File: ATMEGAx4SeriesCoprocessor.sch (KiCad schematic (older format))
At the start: 8 parts, among them J2 AVR-ISP-6, J3 Conn_01x06 (Serial Connector)

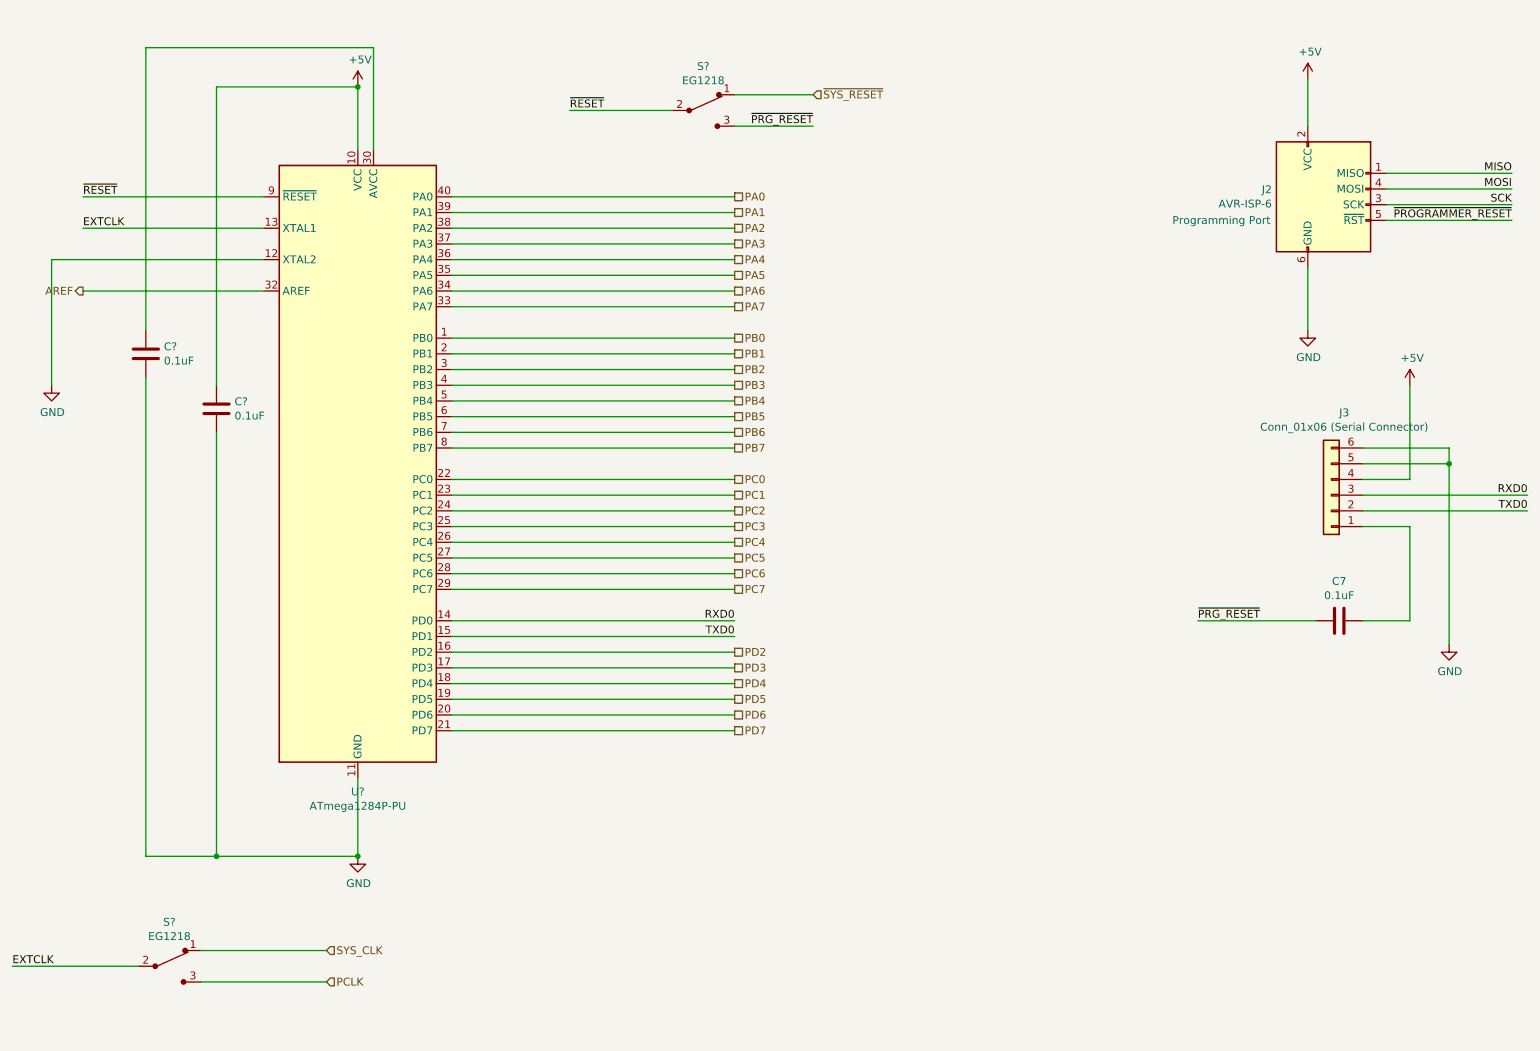
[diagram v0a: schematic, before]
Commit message: ATMEGAx4 coprocessor is basically setup
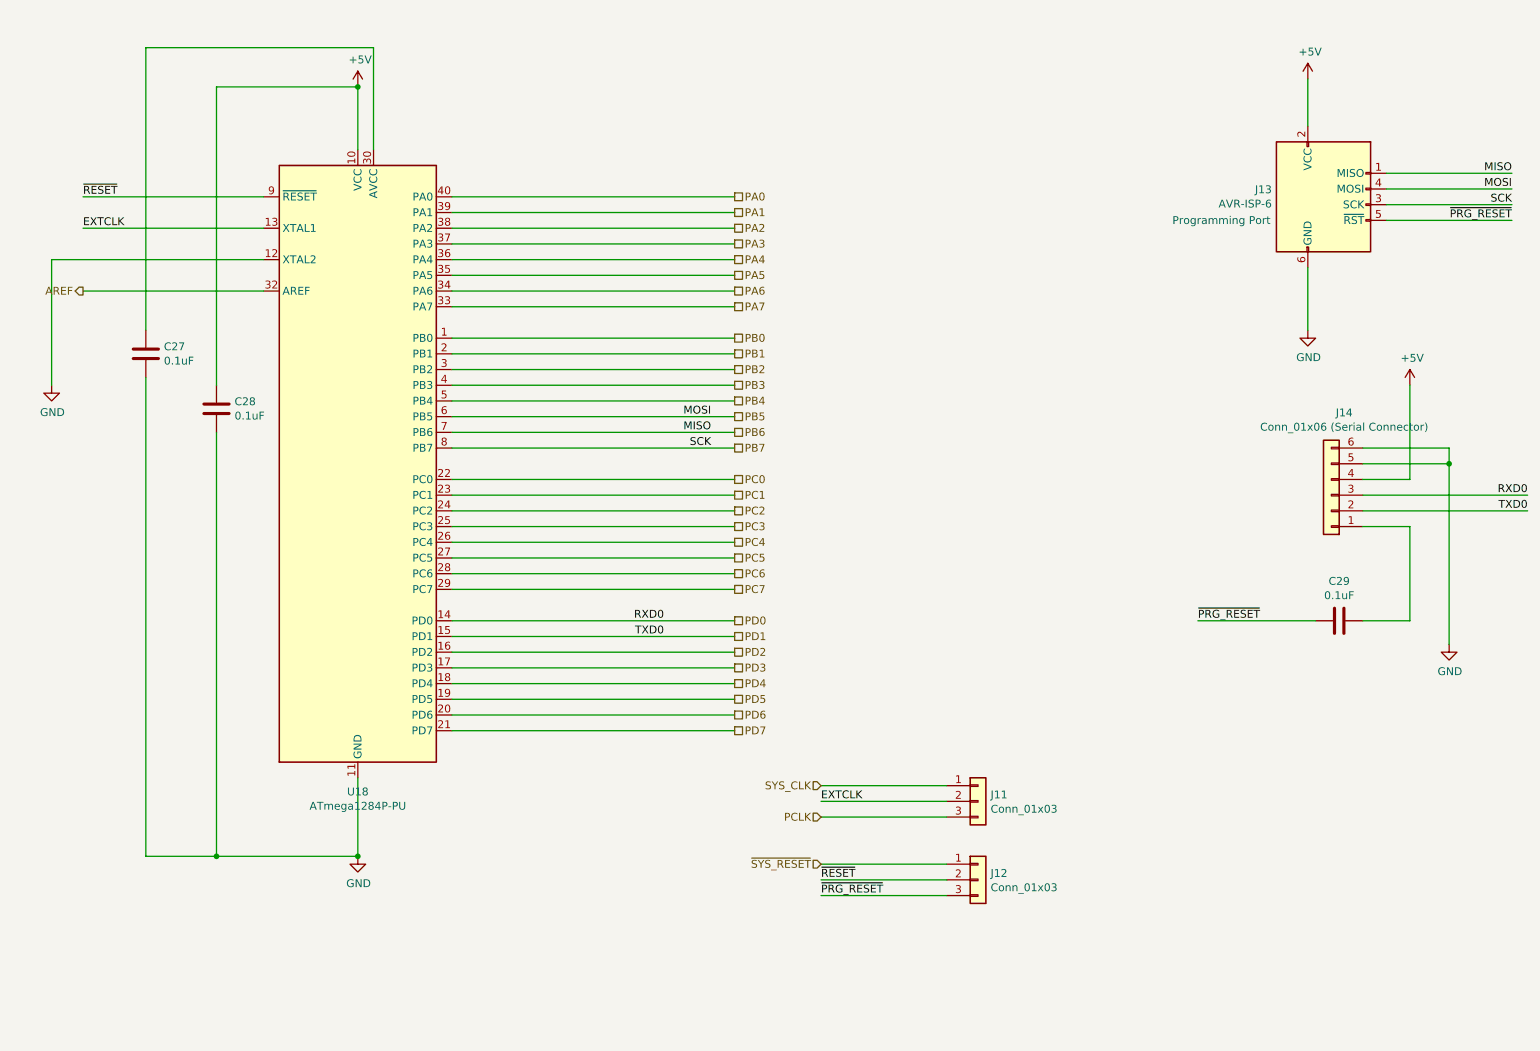
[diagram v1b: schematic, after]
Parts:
- removed S? (x2): EG1218, digikey-footprints:Switch_Slide_11.6x4mm_EG1218, symbol dk_Slide-Switches:EG1218
- added J11, J12: Conn_01x03, Connector_PinHeader_2.54mm:PinHeader_1x03_P2.54mm_Vertical, symbol Connector_Generic:Conn_01x03
- gave numbers to parts that had none: 3
- renumbered C7 to C29, J2 to J13, J3 to J14
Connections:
- net MISO is gone; now on net PB6: J13.1 (MISO)
- net MOSI is gone; now on net PB5: J13.4 (MOSI)
- net SCK is gone; now on net PB7: J13.3 (SCK)
- net ~PROGRAMMER_RESET is gone; now on net ~PRG_RESET: J13.5 (~RST)
- net EXTCLK: now also J11.2 (Pin_2)
- net PCLK: now also J11.3 (Pin_3)
- net SYS_CLK: now also J11.1 (Pin_1)
- net ~PRG_RESET: now also J12.3 (Pin_3)
- net ~RESET: now also J12.2 (Pin_2)
- net ~SYS_RESET: now also J12.1 (Pin_1)
- net RXD0 renamed PD0
- net TXD0 renamed PD1
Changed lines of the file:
@@
 $Descr A4 11693 8268
 encoding utf-8
-Sheet 4 2
+Sheet 2 2
 Title ""
 Date ""
@@
 $EndDescr
 $Comp
-L MCU_Microchip_ATmega:ATmega1284P-PU U?
+L MCU_Microchip_ATmega:ATmega1284P-PU U18
 U 1 1 7D8FC773
 P 3400 3250
-F 0 "U?" H 3400 1161 50  0000 C CNN
+F 0 "U18" H 3400 1161 50  0000 C CNN
 F 1 "ATmega1284P-PU" H 3400 1070 50  0000 C CNN
 F 2 "Package_DIP:DIP-40_W15.24mm_Socket" H 3400 3250 50  0001 C CIN
@@
 Connection ~ 3400 850
 $Comp
-L power:+5V #PWR?
+L power:+5V #PWR066
 U 1 1 7D8FC77F
 P 3400 850
-F 0 "#PWR?" H 3400 700 50  0001 C CNN
+F 0 "#PWR066" H 3400 700 50  0001 C CNN
 F 1 "+5V" H 3415 1023 50  0000 C CNN
 F 2 "" H 3400 850 50  0001 C CNN
@@
 $EndComp
 $Comp
-L power:GND #PWR?
+L power:GND #PWR067
 U 1 1 7D8FC785
 P 3400 5750
-F 0 "#PWR?" H 3400 5500 50  0001 C CNN
+F 0 "#PWR067" H 3400 5500 50  0001 C CNN
 F 1 "GND" H 3405 5577 50  0000 C CNN
 F 2 "" H 3400 5750 50  0001 C CNN
@@
 Connection ~ 3400 5750
 $Comp
-L Device:C C?
+L Device:C C27
 U 1 1 7D8FC78C
 P 2050 2550
-F 0 "C?" H 2165 2596 50  0000 L CNN
+F 0 "C27" H 2165 2596 50  0000 L CNN
 F 1 "0.1uF" H 2165 2505 50  0000 L CNN
 F 2 "" H 2088 2400 50  0001 C CNN
@@
 Connection ~ 2500 5750
 $Comp
-L Device:C C?
+L Device:C C28
 U 1 1 7D8FC798
 P 2500 2900
-F 0 "C?" H 2615 2946 50  0000 L CNN
+F 0 "C28" H 2615 2946 50  0000 L CNN
 F 1 "0.1uF" H 2615 2855 50  0000 L CNN
 F 2 "" H 2538 2750 50  0001 C CNN
@@
 	2500 3050 2500 5750
 $Comp
-L power:GND #PWR?
+L power:GND #PWR065
 U 1 1 7D8FC79F
 P 1450 2750
-F 0 "#PWR?" H 1450 2500 50  0001 C CNN
+F 0 "#PWR065" H 1450 2500 50  0001 C CNN
 F 1 "GND" H 1455 2577 50  0000 C CNN
 F 2 "" H 1450 2750 50  0001 C CNN
@@
 Wire Wire Line
 	2800 1750 1650 1750
-Text HLabel 3200 6350 2    50   Input ~ 0
+Text HLabel 6350 5300 0    50   Input ~ 0
 SYS_CLK
 Wire Wire Line
@@
 Text HLabel 5800 2850 2    50   UnSpc ~ 0
 PB4
-Text HLabel 5800 2950 2    50   UnSpc ~ 0
-PB5
-Text HLabel 5800 3050 2    50   UnSpc ~ 0
-PB6
-Text HLabel 5800 3150 2    50   UnSpc ~ 0
-PB7
 Text HLabel 5800 3350 2    50   UnSpc ~ 0
 PC0
@@
 PD7
 $Comp
-L Connector:AVR-ISP-6 J2
+L Connector:AVR-ISP-6 J13
 U 1 1 65D0C082
 P 9550 1600
-F 0 "J2" H 9221 1696 50  0000 R CNN
+F 0 "J13" H 9221 1696 50  0000 R CNN
 F 1 "AVR-ISP-6" H 9221 1605 50  0000 R CNN
 F 2 "Connector_PinHeader_2.54mm:PinHeader_2x03_P2.54mm_Vertical" V 9300 1650 50  0001 C CNN
@@
 	1    0    0    -1
 $EndComp
-Text Label 10750 1400 2    50   ~ 0
-MISO
 Text Label 10750 1500 2    50   ~ 0
 MOSI
@@
 	9450 1100 9450 800
 $Comp
-L power:+5V #PWR022
+L power:+5V #PWR068
 U 1 1 65D67928
 P 9450 800
-F 0 "#PWR022" H 9450 650 50  0001 C CNN
+F 0 "#PWR068" H 9450 650 50  0001 C CNN
 F 1 "+5V" H 9465 973 50  0000 C CNN
 F 2 "" H 9450 800 50  0001 C CNN
@@
 	9450 2000 9450 2400
 $Comp
-L power:GND #PWR023
+L power:GND #PWR069
 U 1 1 65D7AB96
 P 9450 2400
-F 0 "#PWR023" H 9450 2150 50  0001 C CNN
+F 0 "#PWR069" H 9450 2150 50  0001 C CNN
 F 1 "GND" H 9455 2227 50  0000 C CNN
 F 2 "" H 9450 2400 50  0001 C CNN
@@
 $EndComp
 $Comp
-L Connector_Generic:Conn_01x06 J3
+L Connector_Generic:Conn_01x06 J14
 U 1 1 623C8548
 P 9600 3450
-F 0 "J3" H 9518 2925 50  0000 C CNN
+F 0 "J14" H 9518 2925 50  0000 C CNN
 F 1 "Conn_01x06 (Serial Connector)" H 9518 3016 50  0000 C CNN
 F 2 "Connector_PinHeader_2.54mm:PinHeader_1x06_P2.54mm_Vertical" H 9600 3450 50  0001 C CNN
@@
 	9800 3550 10850 3550
 $Comp
-L power:+5V #PWR026
+L power:+5V #PWR070
 U 1 1 65E08A07
 P 10100 2750
-F 0 "#PWR026" H 10100 2600 50  0001 C CNN
+F 0 "#PWR070" H 10100 2600 50  0001 C CNN
 F 1 "+5V" H 10115 2923 50  0000 C CNN
 F 2 "" H 10100 2750 50  0001 C CNN
@@
 	9800 3350 10100 3350
 $Comp
-L power:GND #PWR027
+L power:GND #PWR071
 U 1 1 65DF3F8A
 P 10350 4400
-F 0 "#PWR027" H 10350 4150 50  0001 C CNN
+F 0 "#PWR071" H 10350 4150 50  0001 C CNN
 F 1 "GND" H 10355 4227 50  0000 C CNN
 F 2 "" H 10350 4400 50  0001 C CNN
@@
 	8750 4250 9500 4250
 $Comp
-L Device:C C7
+L Device:C C29
 U 1 1 65D916C2
 P 9650 4250
-F 0 "C7" V 9398 4250 50  0000 C CNN
+F 0 "C29" V 9398 4250 50  0000 C CNN
 F 1 "0.1uF" V 9489 4250 50  0000 C CNN
 F 2 "Capacitor_SMD:C_0805_2012Metric_Pad1.18x1.45mm_HandSolder" H 9688 4100 50  0001 C CNN
@@
 Text Label 8750 4250 0    50   ~ 0
 ~PRG_RESET
-Text Label 4750 1000 0    50   ~ 0
-~RESET
 Text Label 10750 1700 2    50   ~ 0
-~PROGRAMMER_RESET
+~PRG_RESET
 Wire Wire Line
 	9950 1700 10750 1700
@@
 Wire Wire Line
 	9950 1400 10750 1400
-Text HLabel 6300 900  2    50   Input ~ 0
+Text HLabel 6350 5800 0    50   Input ~ 0
 ~SYS_RESET
 Text Label 1650 1550 0    50   ~ 0
 ~RESET
-Text Label 5800 4250 2    50   ~ 0
+Text Label 5350 4250 2    50   ~ 0
 RXD0
-Text Label 5800 4350 2    50   ~ 0
+Text Label 5350 4350 2    50   ~ 0
 TXD0
 Wire Wire Line
-	2400 6350 3200 6350
-Wire Wire Line
-	2000 6450 1200 6450
-Text Label 1200 6450 0    50   ~ 0
+	7150 5400 6350 5400
+Text Label 6350 5400 0    50   ~ 0
 EXTCLK
 Text Label 1650 1750 0    50   ~ 0
 EXTCLK
-$Comp
-L dk_Slide-Switches:EG1218 S?
-U 1 1 7D9E5966
-P 2200 6450
-F 0 "S?" H 2200 6731 50  0000 C CNN
-F 1 "EG1218" H 2200 6640 50  0000 C CNN
-F 2 "digikey-footprints:Switch_Slide_11.6x4mm_EG1218" H 2400 6650 50  0001 L CNN
-F 3 "http://spec_sheets.e-switch.com/specs/P040040.pdf" H 2400 6750 60  0001 L CNN
-F 4 "EG1903-ND" H 2400 6850 60  0001 L CNN "Digi-Key_PN"
-F 5 "EG1218" H 2400 6950 60  0001 L CNN "MPN"
-F 6 "Switches" H 2400 7050 60  0001 L CNN "Category"
-F 7 "Slide Switches" H 2400 7150 60  0001 L CNN "Family"
-F 8 "http://spec_sheets.e-switch.com/specs/P040040.pdf" H 2400 7250 60  0001 L CNN "DK_Datasheet_Link"
-F 9 "/product-detail/en/e-switch/EG1218/EG1903-ND/101726" H 2400 7350 60  0001 L CNN "DK_Detail_Page"
-F 10 "SWITCH SLIDE SPDT 200MA 30V" H 2400 7450 60  0001 L CNN "Description"
-F 11 "E-Switch" H 2400 7550 60  0001 L CNN "Manufacturer"
-F 12 "Active" H 2400 7650 60  0001 L CNN "Status"
-	1    2200 6450
-	1    0    0    -1
-$EndComp
-Wire Wire Line
-	2400 6550 3200 6550
-Text HLabel 3200 6550 2    50   Input ~ 0
+Text HLabel 6350 5500 0    50   Input ~ 0
 PCLK
-$Comp
-L dk_Slide-Switches:EG1218 S?
-U 1 1 7D9EE15A
-P 5600 1000
-F 0 "S?" H 5600 1281 50  0000 C CNN
-F 1 "EG1218" H 5600 1190 50  0000 C CNN
-F 2 "digikey-footprints:Switch_Slide_11.6x4mm_EG1218" H 5800 1200 50  0001 L CNN
-F 3 "http://spec_sheets.e-switch.com/specs/P040040.pdf" H 5800 1300 60  0001 L CNN
-F 4 "EG1903-ND" H 5800 1400 60  0001 L CNN "Digi-Key_PN"
-F 5 "EG1218" H 5800 1500 60  0001 L CNN "MPN"
-F 6 "Switches" H 5800 1600 60  0001 L CNN "Category"
-F 7 "Slide Switches" H 5800 1700 60  0001 L CNN "Family"
-F 8 "http://spec_sheets.e-switch.com/specs/P040040.pdf" H 5800 1800 60  0001 L CNN "DK_Datasheet_Link"
-F 9 "/product-detail/en/e-switch/EG1218/EG1903-ND/101726" H 5800 1900 60  0001 L CNN "DK_Detail_Page"
-F 10 "SWITCH SLIDE SPDT 200MA 30V" H 5800 2000 60  0001 L CNN "Description"
-F 11 "E-Switch" H 5800 2100 60  0001 L CNN "Manufacturer"
-F 12 "Active" H 5800 2200 60  0001 L CNN "Status"
-	1    5600 1000
-	1    0    0    -1
-$EndComp
-Wire Wire Line
-	4750 1000 5400 1000
-Wire Wire Line
-	5800 900  6300 900
-Wire Wire Line
-	5800 1100 6300 1100
-Text Label 6300 1100 2    50   ~ 0
+Text Label 6350 6000 0    50   ~ 0
 ~PRG_RESET
+Text HLabel 5800 4250 2    50   UnSpc ~ 0
+PD0
+Text HLabel 5800 4350 2    50   UnSpc ~ 0
+PD1
+$Comp
+L Connector_Generic:Conn_01x03 J11
+U 1 1 7DB0129D
+P 7350 5400
+F 0 "J11" H 7430 5442 50  0000 L CNN
+F 1 "Conn_01x03" H 7430 5351 50  0000 L CNN
+F 2 "Connector_PinHeader_2.54mm:PinHeader_1x03_P2.54mm_Vertical" H 7350 5400 50  0001 C CNN
+F 3 "~" H 7350 5400 50  0001 C CNN
+	1    7350 5400
+	1    0    0    -1
+$EndComp
+Wire Wire Line
+	6350 5300 7150 5300
+Wire Wire Line
+	7150 5500 6350 5500
+Wire Wire Line
+	7150 5900 6350 5900
+Text Label 6350 5900 0    50   ~ 0
+~RESET
+$Comp
+L Connector_Generic:Conn_01x03 J12
+U 1 1 7DB0C2C2
+P 7350 5900
+F 0 "J12" H 7430 5942 50  0000 L CNN
+F 1 "Conn_01x03" H 7430 5851 50  0000 L CNN
+F 2 "Connector_PinHeader_2.54mm:PinHeader_1x03_P2.54mm_Vertical" H 7350 5900 50  0001 C CNN
+F 3 "~" H 7350 5900 50  0001 C CNN
+	1    7350 5900
+	1    0    0    -1
+$EndComp
+Wire Wire Line
+	6350 5800 7150 5800
+Wire Wire Line
+	7150 6000 6350 6000
+Text Label 10750 1400 2    50   ~ 0
+MISO
+Text HLabel 5800 3050 2    50   UnSpc ~ 0
+PB6
+Text HLabel 5800 3150 2    50   UnSpc ~ 0
+PB7
+Text HLabel 5800 2950 2    50   UnSpc ~ 0
+PB5
+Text Label 5650 3150 2    50   ~ 0
+SCK
+Text Label 5650 2950 2    50   ~ 0
+MOSI
+Text Label 5650 3050 2    50   ~ 0
+MISO
 $EndSCHEMATC

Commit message: Partially pinout the extra x4 hardware
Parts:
- C27, C28: footprint (none) -> Capacitor_SMD:C_0805_2012Metric_Pad1.18x1.45mm_HandSolder
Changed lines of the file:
@@
 F 0 "C27" H 2165 2596 50  0000 L CNN
 F 1 "0.1uF" H 2165 2505 50  0000 L CNN
-F 2 "" H 2088 2400 50  0001 C CNN
+F 2 "Capacitor_SMD:C_0805_2012Metric_Pad1.18x1.45mm_HandSolder" H 2088 2400 50  0001 C CNN
 F 3 "~" H 2050 2550 50  0001 C CNN
 	1    2050 2550
@@
 F 0 "C28" H 2615 2946 50  0000 L CNN
 F 1 "0.1uF" H 2615 2855 50  0000 L CNN
-F 2 "" H 2538 2750 50  0001 C CNN
+F 2 "Capacitor_SMD:C_0805_2012Metric_Pad1.18x1.45mm_HandSolder" H 2538 2750 50  0001 C CNN
 F 3 "~" H 2500 2900 50  0001 C CNN
 	1    2500 2900

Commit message: Move the coprocessor clock source selector to the main page
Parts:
- removed J11: Conn_01x03, Connector_PinHeader_2.54mm:PinHeader_1x03_P2.54mm_Vertical, symbol Connector_Generic:Conn_01x03
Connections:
- net EXTCLK renamed CLK
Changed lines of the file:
@@
 Wire Wire Line
 	2800 1750 1650 1750
-Text HLabel 6350 5300 0    50   Input ~ 0
-SYS_CLK
 Wire Wire Line
 	4000 1550 5800 1550
@@
 Text Label 5350 4350 2    50   ~ 0
 TXD0
-Wire Wire Line
-	7150 5400 6350 5400
-Text Label 6350 5400 0    50   ~ 0
-EXTCLK
-Text Label 1650 1750 0    50   ~ 0
-EXTCLK
-Text HLabel 6350 5500 0    50   Input ~ 0
-PCLK
 Text Label 6350 6000 0    50   ~ 0
 ~PRG_RESET
@@
 Text HLabel 5800 4350 2    50   UnSpc ~ 0
 PD1
-$Comp
-L Connector_Generic:Conn_01x03 J11
-U 1 1 7DB0129D
-P 7350 5400
-F 0 "J11" H 7430 5442 50  0000 L CNN
-F 1 "Conn_01x03" H 7430 5351 50  0000 L CNN
-F 2 "Connector_PinHeader_2.54mm:PinHeader_1x03_P2.54mm_Vertical" H 7350 5400 50  0001 C CNN
-F 3 "~" H 7350 5400 50  0001 C CNN
-	1    7350 5400
-	1    0    0    -1
-$EndComp
-Wire Wire Line
-	6350 5300 7150 5300
-Wire Wire Line
-	7150 5500 6350 5500
 Wire Wire Line
 	7150 5900 6350 5900
@@
 Text Label 5650 3050 2    50   ~ 0
 MISO
+Text HLabel 1650 1750 0    50   Input ~ 0
+CLK
 $EndSCHEMATC
